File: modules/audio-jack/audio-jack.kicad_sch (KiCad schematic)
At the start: 1 part, among them J1 SJ-43514-SMT-TR

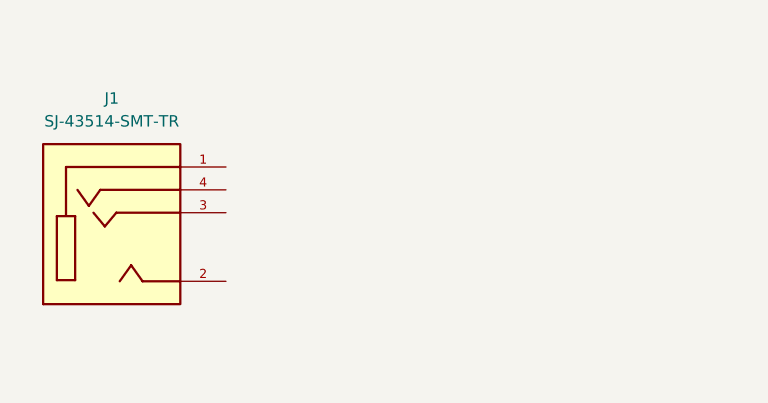
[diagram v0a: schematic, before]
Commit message: finish audio jack module
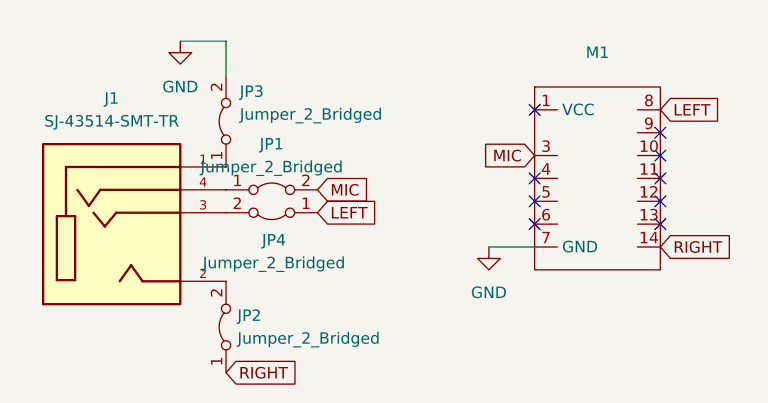
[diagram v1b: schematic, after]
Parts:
- added JP1, JP2, JP3, JP4: Jumper_2_Bridged, Jumper:SolderJumper-2_P1.3mm_Bridged_RoundedPad1.0x1.5mm, symbol Jumper:Jumper_2_Bridged
- added M1: ~, MegaCastle:MegaCastle2x7-Module-I12.7x11.5-MA304, symbol MegaCastle:MegaCastle2x7-Module
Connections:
- net at J1.1: now also JP3.1 (A)
- net at J1.2: now also JP2.2 (B)
- net at J1.3: now also JP4.2 (B)
- net at J1.4: now also JP1.1 (A)
- new net GND: JP3.2 (B), M1.7 (GND)
- new net LEFT: JP4.1 (A), M1.8
- new net MIC: JP1.2 (B), M1.3
- new net RIGHT: JP2.1 (A), M1.14
- no-connect marks 0 -> 9

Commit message: update audio-jack PCB to include panel
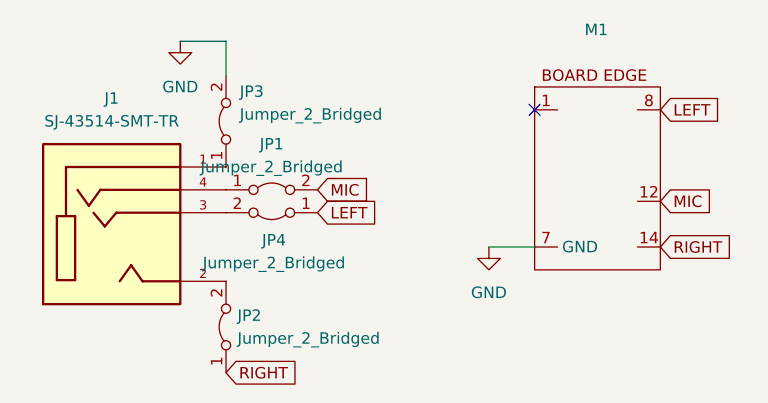
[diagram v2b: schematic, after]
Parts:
- removed M1: ~, MegaCastle:MegaCastle2x7-Module-I12.7x11.5-MA304, symbol MegaCastle:MegaCastle2x7-Module
- added M1: ~, MegaCastle:MegaCastle2x7-Module-I12.7x13.0-M8314-PANEL-NIBBLE, symbol MegaCastle:MegaCastle2x7-Module-I12.7x13.0-M8314-NOCUTOUT-EDGE
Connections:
- net GND: now also M1.7 (GND)
- net LEFT: now also M1.8
- net MIC: now also M1.12
- net RIGHT: now also M1.14
- no-connect marks 9 -> 1
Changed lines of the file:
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@@
 	(paper "A4")
 	(no_connect
-		(at 128.27 55.88)
-	)
-	(no_connect
-		(at 128.27 53.34)
-	)
-	(no_connect
-		(at 114.3 53.34)
-	)
-	(no_connect
-		(at 114.3 55.88)
-	)
-	(no_connect
-		(at 128.27 48.26)
-	)
-	(no_connect
-		(at 128.27 58.42)
-	)
-	(no_connect
-		(at 128.27 50.8)
-	)
-	(no_connect
 		(at 114.3 45.72)
-	)
-	(no_connect
-		(at 114.3 58.42)
 	)
 	(wire
@@
 	(global_label "MIC"
 		(shape input)
-		(at 114.3 50.8 180)
+		(at 128.27 55.88 0)
 		(fields_autoplaced yes)
 		(effects
@@
 				(size 1.27 1.27)
 			)
-			(justify right)
+			(justify left)
 		)
 		(property "Intersheetrefs" "${INTERSHEET_REFS}"
-			(at 107.9886 50.8 0)
-			(effects
-				(font
-					(size 1.27 1.27)
-				)
-				(justify right)
+			(at 134.5814 55.88 0)
+			(effects
+				(font
+					(size 1.27 1.27)
+				)
+				(justify left)
 				(hide yes)
 			)
@@
 				(justify left)
 				(hide yes)
-			)
-		)
-	)
-	(symbol
-		(lib_id "MegaCastle:MegaCastle2x7-Module")
-		(at 120.65 57.15 0)
-		(unit 1)
-		(exclude_from_sim no)
-		(in_bom yes)
-		(on_board yes)
-		(dnp no)
-		(fields_autoplaced yes)
-		(property "Reference" "M1"
-			(at 121.285 39.37 0)
-			(effects
-				(font
-					(size 1.27 1.27)
-				)
-			)
-		)
-		(property "Value" "~"
-			(at 121.285 41.91 0)
-			(effects
-				(font
-					(size 1.27 1.27)
-				)
-			)
-		)
-		(property "Footprint" "MegaCastle:MegaCastle2x7-Module-I12.7x11.5-MA304"
-			(at 120.65 52.07 0)
-			(effects
-				(font
-					(size 1.27 1.27)
-				)
-				(hide yes)
-			)
-		)
-		(property "Datasheet" ""
-			(at 120.65 52.07 0)
-			(effects
-				(font
-					(size 1.27 1.27)
-				)
-				(hide yes)
-			)
-		)
-		(property "Description" ""
-			(at 120.65 57.15 0)
-			(effects
-				(font
-					(size 1.27 1.27)
-				)
-				(hide yes)
-			)
-		)
-		(pin "3"
-		)
-		(pin "4"
-		)
-		(pin "6"
-		)
-		(pin "7"
-		)
-		(pin "1"
-		)
-		(pin "11"
-		)
-		(pin "8"
-		)
-		(pin "9"
-		)
-		(pin "5"
-		)
-		(pin "13"
-		)
-		(pin "12"
-		)
-		(pin "10"
-		)
-		(pin "14"
-		)
-		(instances
-			(project ""
-				(path "/11c40d59-ce80-46cc-9a27-56abc67b9c9a"
-					(reference "M1")
-					(unit 1)
-				)
 			)
 		)
@@
 					(unit 1)
 				)
+			)
+		)
+	)
+	(symbol
+		(lib_id "MegaCastle:MegaCastle2x7-Module-I12.7x13.0-M8314-NOCUTOUT-EDGE")
+		(at 120.65 53.34 0)
+		(unit 1)
+		(exclude_from_sim no)
+		(in_bom yes)
+		(on_board yes)
+		(dnp no)
+		(fields_autoplaced yes)
+		(property "Reference" "M1"
+			(at 121.1538 36.83 0)
+			(effects
+				(font
+					(size 1.27 1.27)
+				)
+			)
+		)
+		(property "Value" "~"
+			(at 121.1538 39.37 0)
+			(effects
+				(font
+					(size 1.27 1.27)
+				)
+			)
+		)
+		(property "Footprint" "MegaCastle:MegaCastle2x7-Module-I12.7x13.0-M8314-PANEL-NIBBLE"
+			(at 120.65 68.58 0)
+			(effects
+				(font
+					(size 1.27 1.27)
+				)
+				(hide yes)
+			)
+		)
+		(property "Datasheet" ""
+			(at 120.65 48.26 0)
+			(effects
+				(font
+					(size 1.27 1.27)
+				)
+				(hide yes)
+			)
+		)
+		(property "Description" "Generated using footprint-gen .. 12.7 11.5 5 2"
+			(at 120.65 53.34 0)
+			(effects
+				(font
+					(size 1.27 1.27)
+				)
+				(hide yes)
+			)
+		)
+		(pin "8"
+		)
+		(pin "12"
+		)
+		(pin "1"
+		)
+		(pin "14"
+		)
+		(pin "7"
+		)
+		(instances
+			(project ""
+				(path "/11c40d59-ce80-46cc-9a27-56abc67b9c9a"
+					(reference "M1")
+					(unit 1)
+				)
